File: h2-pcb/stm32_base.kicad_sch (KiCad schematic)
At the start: 41 parts, among them J1 Network Connector, J2 STDC14, SW1 SW_Push, U1 LD39050PU33R, U2 STM32G474RBT6, U3 SN65HVD230, Y1 8MHz

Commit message: Added Mosfets and LEDs
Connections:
- net PA6: now reaches U2.20 (PA6)
- net PA7: now reaches U2.21 (PA7)
- net PB0: now reaches U2.24 (PB0)
- net PB1: now reaches U2.25 (PB1)
- net PB2: now reaches U2.26 (PB2)
- net PA8: now reaches U2.42 (PA8)
- no-connect marks 37 -> 31
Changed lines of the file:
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@@
-	)
-	(no_connect
-		(at 99.06 110.49)
 	)
 	(no_connect
@@
 	)
 	(no_connect
-		(at 99.06 143.51)
-	)
-	(no_connect
 		(at 99.06 163.83)
 	)
@@
 	)
 	(no_connect
-		(at 99.06 115.57)
-	)
-	(no_connect
 		(at 63.5 138.43)
 	)
@@
 	)
 	(no_connect
-		(at 99.06 140.97)
-	)
-	(no_connect
-		(at 99.06 138.43)
-	)
-	(no_connect
 		(at 99.06 176.53)
 	)
@@
 	)
 	(no_connect
-		(at 99.06 113.03)
-	)
-	(no_connect
 		(at 99.06 161.29)
 	)
@@
 	(wire
 		(pts
+			(xy 99.06 118.11) (xy 101.6 118.11)
+		)
+		(stroke
+			(width 0)
+			(type default)
+		)
+	)
+	(wire
+		(pts
 			(xy 99.06 102.87) (xy 115.57 102.87)
 		)
@@
 	(wire
 		(pts
-			(xy 99.06 118.11) (xy 101.6 118.11)
-		)
-		(stroke
-			(width 0)
-			(type default)
-		)
-	)
-	(wire
-		(pts
 			(xy 146.05 142.24) (xy 146.05 143.51)
 		)
@@
 	(wire
 		(pts
+			(xy 99.06 143.51) (xy 101.6 143.51)
+		)
+		(stroke
+			(width 0)
+			(type default)
+		)
+	)
+	(wire
+		(pts
 			(xy 276.86 90.17) (xy 260.35 90.17)
 		)
@@
 	(wire
 		(pts
+			(xy 99.06 140.97) (xy 101.6 140.97)
+		)
+		(stroke
+			(width 0)
+			(type default)
+		)
+	)
+	(wire
+		(pts
 			(xy 276.86 107.95) (xy 260.35 107.95)
 		)
@@
 	(wire
 		(pts
+			(xy 99.06 113.03) (xy 101.6 113.03)
+		)
+		(stroke
+			(width 0)
+			(type default)
+		)
+	)
+	(wire
+		(pts
 			(xy 135.89 74.93) (xy 135.89 76.2)
 		)
@@
 	(wire
 		(pts
+			(xy 99.06 115.57) (xy 101.6 115.57)
+		)
+		(stroke
+			(width 0)
+			(type default)
+		)
+	)
+	(wire
+		(pts
 			(xy 83.82 87.63) (xy 83.82 86.36)
 		)
@@
 	(wire
 		(pts
+			(xy 99.06 110.49) (xy 101.6 110.49)
+		)
+		(stroke
+			(width 0)
+			(type default)
+		)
+	)
+	(wire
+		(pts
 			(xy 135.89 142.24) (xy 137.16 142.24)
 		)
@@
 		(pts
 			(xy 109.22 158.75) (xy 109.22 160.02)
+		)
+		(stroke
+			(width 0)
+			(type default)
+		)
+	)
+	(wire
+		(pts
+			(xy 99.06 138.43) (xy 101.6 138.43)
 		)
 		(stroke
@@
 			)
 			(justify right bottom)
+		)
+	)
+	(hierarchical_label "PB2"
+		(shape output)
+		(at 101.6 143.51 0)
+		(effects
+			(font
+				(size 1.27 1.27)
+			)
+			(justify left)
 		)
 	)
@@
 		)
 	)
+	(hierarchical_label "PA6"
+		(shape output)
+		(at 101.6 110.49 0)
+		(effects
+			(font
+				(size 1.27 1.27)
+			)
+			(justify left)
+		)
+	)
+	(hierarchical_label "PA8"
+		(shape output)
+		(at 101.6 115.57 0)
+		(effects
+			(font
+				(size 1.27 1.27)
+			)
+			(justify left)
+		)
+	)
+	(hierarchical_label "PA7"
+		(shape output)
+		(at 101.6 113.03 0)
+		(effects
+			(font
+				(size 1.27 1.27)
+			)
+			(justify left)
+		)
+	)
 	(hierarchical_label "PA9"
 		(shape output)
@@
 		)
 	)
+	(hierarchical_label "PB1"
+		(shape output)
+		(at 101.6 140.97 0)
+		(effects
+			(font
+				(size 1.27 1.27)
+			)
+			(justify left)
+		)
+	)
 	(hierarchical_label "PA5"
 		(shape output)
@@
 		(effects
 			(font
+				(size 1.27 1.27)
+			)
+			(justify left)
+		)
+	)
+	(hierarchical_label "PB0"
+		(shape output)
+		(at 101.6 138.43 0)
+		(effects
+			(font

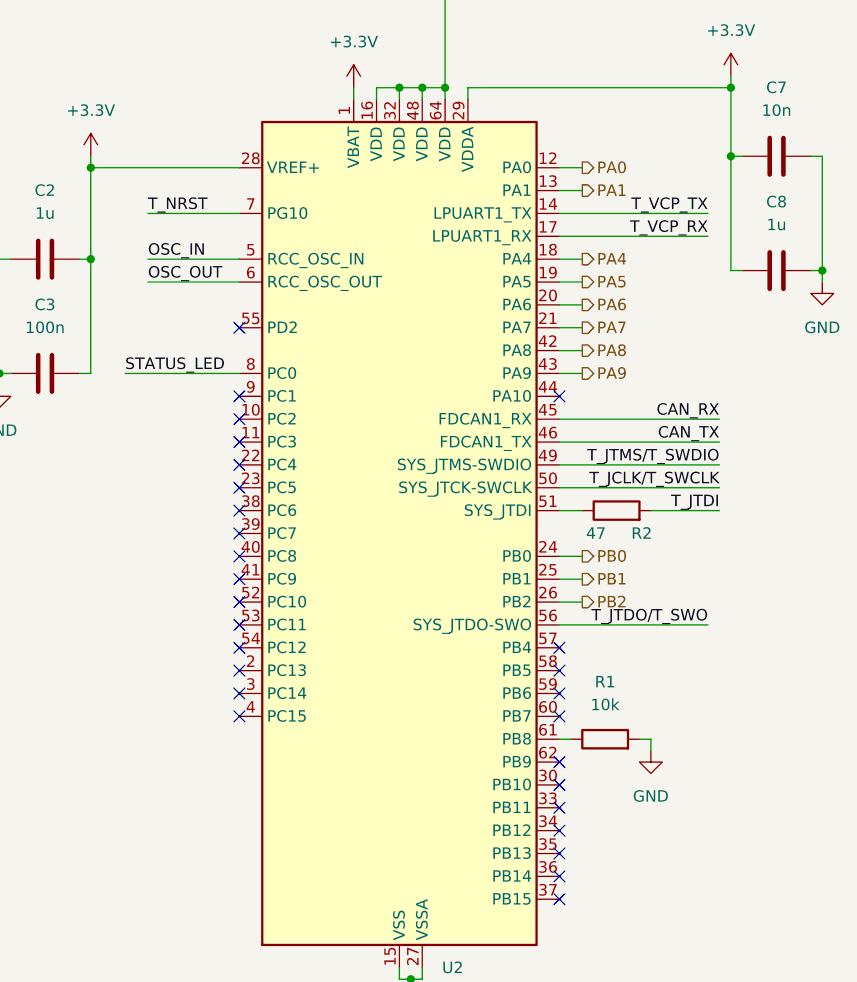
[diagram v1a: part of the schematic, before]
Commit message: h2-pcb: implement review comments in schematic
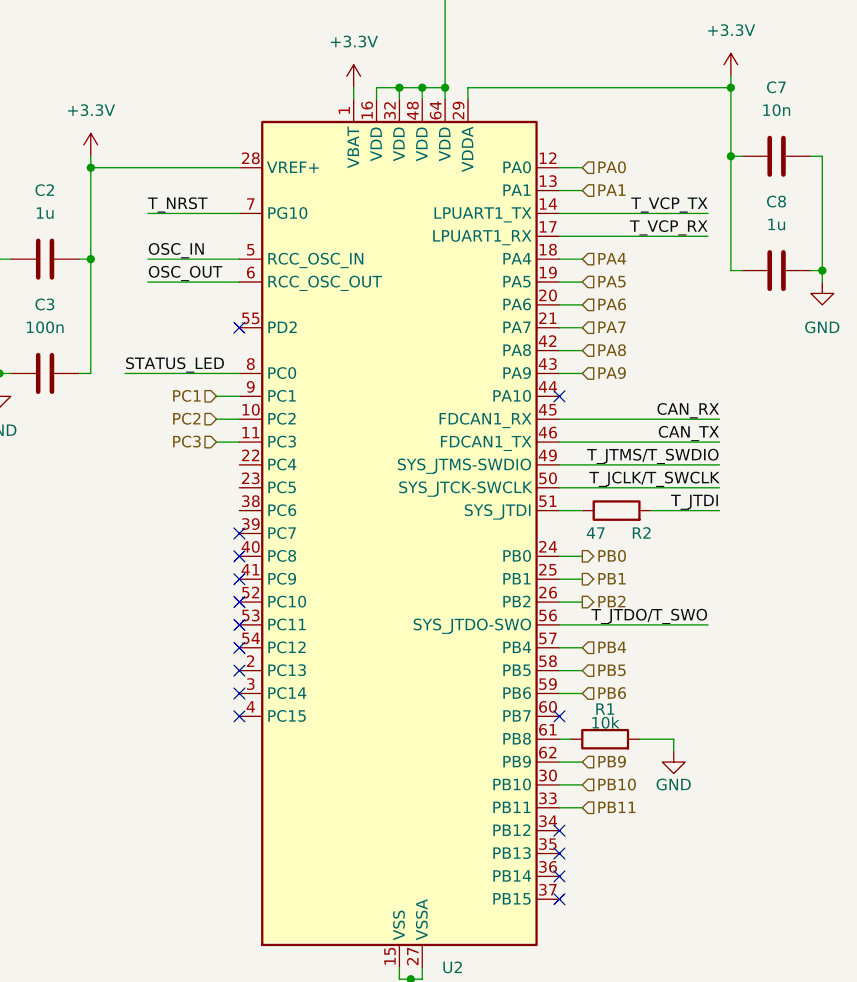
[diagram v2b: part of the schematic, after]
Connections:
- net PC2: now reaches U2.10 (PC2)
- net PC3: now reaches U2.11 (PC3)
- net PB10: now reaches U2.30 (PB10)
- net PB11: now reaches U2.33 (PB11)
- net PB4: now reaches U2.57 (PB4)
- net PB5: now reaches U2.58 (PB5)
- net PB6: now reaches U2.59 (PB6)
- net PB9: now reaches U2.62 (PB9)
- net PC1: now reaches U2.9 (PC1)
- no-connect marks 31 -> 19
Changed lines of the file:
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@@
 	)
 	(no_connect
-		(at 99.06 163.83)
-	)
-	(no_connect
 		(at 99.06 120.65)
 	)
 	(no_connect
-		(at 99.06 148.59)
-	)
-	(no_connect
 		(at 260.35 100.33)
 	)
@@
 	)
 	(no_connect
-		(at 99.06 151.13)
-	)
-	(no_connect
 		(at 74.93 31.75)
 	)
@@
 	)
 	(no_connect
-		(at 99.06 153.67)
-	)
-	(no_connect
-		(at 63.5 128.27)
-	)
-	(no_connect
-		(at 63.5 120.65)
-	)
-	(no_connect
-		(at 63.5 130.81)
-	)
-	(no_connect
-		(at 63.5 133.35)
-	)
-	(no_connect
 		(at 99.06 176.53)
 	)
@@
 	)
 	(no_connect
-		(at 63.5 125.73)
-	)
-	(no_connect
 		(at 63.5 135.89)
 	)
 	(no_connect
-		(at 99.06 161.29)
-	)
-	(no_connect
-		(at 63.5 123.19)
-	)
-	(no_connect
-		(at 99.06 166.37)
-	)
-	(no_connect
 		(at 99.06 173.99)
 	)
@@
 	(wire
 		(pts
-			(xy 107.95 158.75) (xy 109.22 158.75)
+			(xy 107.95 158.75) (xy 111.76 158.75)
 		)
 		(stroke
@@
 	(wire
 		(pts
+			(xy 99.06 161.29) (xy 101.6 161.29)
+		)
+		(stroke
+			(width 0)
+			(type default)
+		)
+	)
+	(wire
+		(pts
 			(xy 186.69 69.85) (xy 196.85 69.85)
 		)
@@
 	(wire
 		(pts
+			(xy 99.06 163.83) (xy 101.6 163.83)
+		)
+		(stroke
+			(width 0)
+			(type default)
+		)
+	)
+	(wire
+		(pts
 			(xy 243.84 147.32) (xy 243.84 148.59)
 		)
@@
 	(wire
 		(pts
+			(xy 60.96 123.19) (xy 63.5 123.19)
+		)
+		(stroke
+			(width 0)
+			(type default)
+		)
+	)
+	(wire
+		(pts
 			(xy 276.86 107.95) (xy 260.35 107.95)
 		)
@@
 	(wire
 		(pts
+			(xy 60.96 120.65) (xy 63.5 120.65)
+		)
+		(stroke
+			(width 0)
+			(type default)
+		)
+	)
+	(wire
+		(pts
 			(xy 78.74 87.63) (xy 78.74 86.36)
 		)
@@
 	(wire
 		(pts
+			(xy 99.06 148.59) (xy 101.6 148.59)
+		)
+		(stroke
+			(width 0)
+			(type default)
+		)
+	)
+	(wire
+		(pts
 			(xy 135.89 104.14) (xy 137.16 104.14)
 		)
@@
 	(wire
 		(pts
+			(xy 99.06 166.37) (xy 101.6 166.37)
+		)
+		(stroke
+			(width 0)
+			(type default)
+		)
+	)
+	(wire
+		(pts
 			(xy 144.78 116.84) (xy 146.05 116.84)
 		)
@@
 	(wire
 		(pts
+			(xy 60.96 125.73) (xy 63.5 125.73)
+		)
+		(stroke
+			(width 0)
+			(type default)
+		)
+	)
+	(wire
+		(pts
 			(xy 149.86 49.53) (xy 149.86 48.26)
 		)
@@
 	(wire
 		(pts
+			(xy 99.06 153.67) (xy 101.6 153.67)
+		)
+		(stroke
+			(width 0)
+			(type default)
+		)
+	)
+	(wire
+		(pts
 			(xy 83.82 87.63) (xy 83.82 86.36)
 		)
@@
 	(wire
 		(pts
+			(xy 99.06 151.13) (xy 101.6 151.13)
+		)
+		(stroke
+			(width 0)
+			(type default)
+		)
+	)
+	(wire
+		(pts
 			(xy 204.47 69.85) (xy 214.63 69.85)
 		)
@@
 	(wire
 		(pts
-			(xy 109.22 158.75) (xy 109.22 160.02)
+			(xy 111.76 158.75) (xy 111.76 160.02)
 		)
 		(stroke
@@
 		)
 	)
+	(hierarchical_label "PB11"
+		(shape input)
+		(at 101.6 166.37 0)
+		(effects
+			(font
+				(size 1.27 1.27)
+			)
+			(justify left)
+		)
+	)
 	(hierarchical_label "PB2"
 		(shape output)
@@
 	)
 	(hierarchical_label "PA1"
-		(shape output)
+		(shape input)
 		(at 101.6 97.79 0)
 		(effects
@@
 		)
 	)
+	(hierarchical_label "PB5"
+		(shape input)
+		(at 101.6 151.13 0)
+		(effects
+			(font
+				(size 1.27 1.27)
+			)
+			(justify left)
+		)
+	)
+	(hierarchical_label "PC1"
+		(shape input)
+		(at 60.96 120.65 180)
+		(effects
+			(font
+				(size 1.27 1.27)
+			)
+			(justify right)
+		)
+	)
+	(hierarchical_label "PB6"
+		(shape input)
+		(at 101.6 153.67 0)
+		(effects
+			(font
+				(size 1.27 1.27)
+			)
+			(justify left)
+		)
+	)
 	(hierarchical_label "PA6"
-		(shape output)
+		(shape input)
 		(at 101.6 110.49 0)
 		(effects
@@
 	)
 	(hierarchical_label "PA8"
-		(shape output)
+		(shape input)
 		(at 101.6 115.57 0)
 		(effects
@@
 		)
 	)
+	(hierarchical_label "PC2"
+		(shape input)
+		(at 60.96 123.19 180)
+		(effects
+			(font
+				(size 1.27 1.27)
+			)
+			(justify right)
+		)
+	)
 	(hierarchical_label "PA7"
-		(shape output)
+		(shape input)
 		(at 101.6 113.03 0)
 		(effects
@@
 		)
 	)
+	(hierarchical_label "PB9"
+		(shape input)
+		(at 101.6 161.29 0)
+		(effects
+			(font
+				(size 1.27 1.27)
+			)
+			(justify left)
+		)
+	)
 	(hierarchical_label "PA9"
-		(shape output)
+		(shape input)
 		(at 101.6 118.11 0)
 		(effects
@@
 		)
 	)
+	(hierarchical_label "PB10"
+		(shape input)
+		(at 101.6 163.83 0)
+		(effects
+			(font
+				(size 1.27 1.27)
+			)
+			(justify left)
+		)
+	)
 	(hierarchical_label "PA4"
-		(shape output)
+		(shape input)
 		(at 101.6 105.41 0)
 		(effects
@@
 	)
 	(hierarchical_label "PA0"
-		(shape output)
+		(shape input)
 		(at 101.6 95.25 0)
 		(effects
@@
 		)
 	)
+	(hierarchical_label "PC3"
+		(shape input)
+		(at 60.96 125.73 180)
+		(effects
+			(font
+				(size 1.27 1.27)
+			)
+			(justify right)
+		)
+	)
+	(hierarchical_label "PB4"
+		(shape input)
+		(at 101.6 148.59 0)
+		(effects
+			(font
+				(size 1.27 1.27)
+			)
+			(justify left)
+		)
+	)
 	(hierarchical_label "PB1"
 		(shape output)
@@
 	)
 	(hierarchical_label "PA5"
-		(shape output)
+		(shape input)
 		(at 101.6 107.95 0)
 		(effects
@@
 		(on_board yes)
 		(dnp no)
-		(fields_autoplaced yes)
 		(property "Reference" "R1"
-			(at 104.14 152.4 90)
+			(at 104.14 155.448 90)
 			(effects
 				(font
@@
 		)
 		(property "Value" "10k"
-			(at 104.14 154.94 90)
+			(at 104.14 156.972 90)
 			(effects
 				(font
@@
 	(symbol
 		(lib_id "power:GND")
-		(at 109.22 160.02 0)
+		(at 111.76 160.02 0)
 		(unit 1)
 		(exclude_from_sim no)
@@
 		(on_board yes)
 		(dnp no)
-		(fields_autoplaced yes)
 		(property "Reference" "#PWR08"
-			(at 109.22 166.37 0)
+			(at 111.76 166.37 0)
 			(effects
 				(font
@@
 		)
 		(property "Value" "GND"
-			(at 109.22 165.1 0)
+			(at 111.76 163.83 0)
 			(effects
 				(font
@@
 		)
 		(property "Footprint" ""
-			(at 109.22 160.02 0)
+			(at 111.76 160.02 0)
 			(effects
 				(font
@@
 		)
 		(property "Datasheet" ""
-			(at 109.22 160.02 0)
+			(at 111.76 160.02 0)
 			(effects
 				(font
@@
 		)
 		(property "Description" "Power symbol creates a global label with name \"GND\" , ground"
-			(at 109.22 160.02 0)
+			(at 111.76 160.02 0)
 			(effects
 				(font

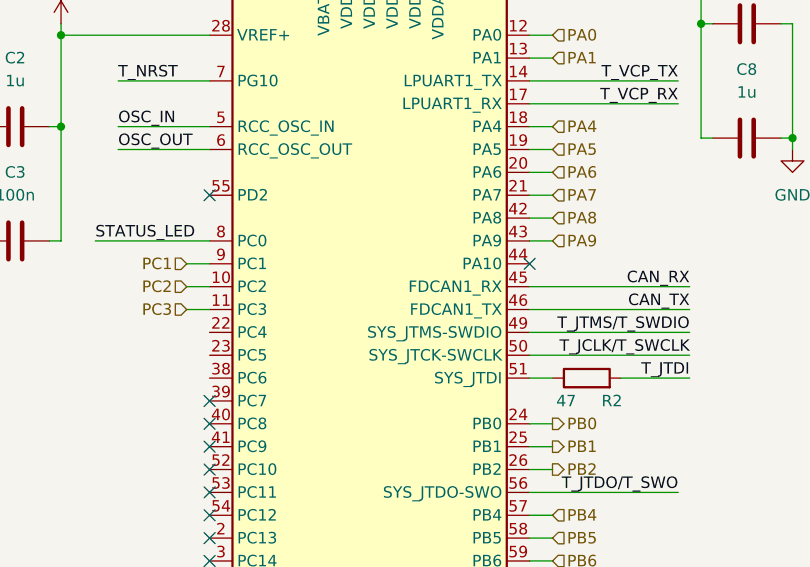
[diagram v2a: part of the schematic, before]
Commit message: h2-pcb: implement review comments in schematic 2.0
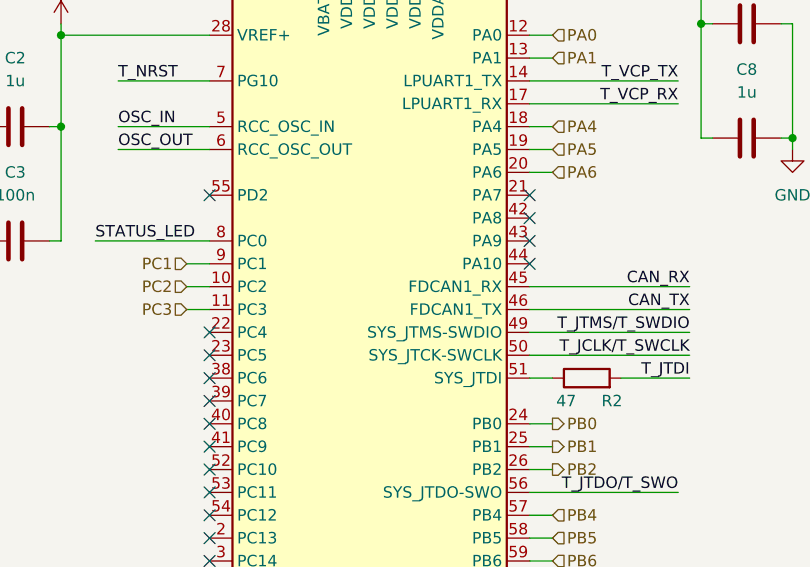
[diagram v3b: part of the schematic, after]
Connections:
- net PA7: no longer names the net of U2.21 (PA7)
- net PA8: no longer names the net of U2.42 (PA8)
- net PA9: no longer names the net of U2.43 (PA9)
- no-connect marks 19 -> 25
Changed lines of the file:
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@@
+	)
+	(no_connect
+		(at 99.06 115.57)
 	)
 	(no_connect
@@
 	)
 	(no_connect
+		(at 63.5 130.81)
+	)
+	(no_connect
 		(at 99.06 171.45)
 	)
@@
 	)
 	(no_connect
+		(at 63.5 128.27)
+	)
+	(no_connect
 		(at 99.06 120.65)
 	)
@@
 	)
 	(no_connect
+		(at 99.06 118.11)
+	)
+	(no_connect
+		(at 63.5 133.35)
+	)
+	(no_connect
 		(at 99.06 176.53)
 	)
@@
 	)
 	(no_connect
+		(at 99.06 113.03)
+	)
+	(no_connect
 		(at 99.06 173.99)
 	)
@@
 	(wire
 		(pts
-			(xy 99.06 118.11) (xy 101.6 118.11)
-		)
-		(stroke
-			(width 0)
-			(type default)
-		)
-	)
-	(wire
-		(pts
 			(xy 99.06 102.87) (xy 115.57 102.87)
 		)
@@
 	(wire
 		(pts
-			(xy 99.06 113.03) (xy 101.6 113.03)
-		)
-		(stroke
-			(width 0)
-			(type default)
-		)
-	)
-	(wire
-		(pts
 			(xy 135.89 74.93) (xy 135.89 76.2)
 		)
@@
 		(pts
 			(xy 81.28 36.83) (xy 81.28 35.56)
-		)
-		(stroke
-			(width 0)
-			(type default)
-		)
-	)
-	(wire
-		(pts
-			(xy 99.06 115.57) (xy 101.6 115.57)
 		)
 		(stroke
@@
 		)
 	)
-	(hierarchical_label "PA8"
-		(shape input)
-		(at 101.6 115.57 0)
-		(effects
-			(font
-				(size 1.27 1.27)
-			)
-			(justify left)
-		)
-	)
 	(hierarchical_label "PC2"
 		(shape input)
@@
 		)
 	)
-	(hierarchical_label "PA7"
-		(shape input)
-		(at 101.6 113.03 0)
-		(effects
-			(font
-				(size 1.27 1.27)
-			)
-			(justify left)
-		)
-	)
 	(hierarchical_label "PB9"
 		(shape input)
@@
 		(effects
 			(font
-				(size 1.27 1.27)
-			)
-			(justify left)
-		)
-	)
-	(hierarchical_label "PA9"
-		(shape input)
-		(at 101.6 118.11 0)
-		(effects
-			(font

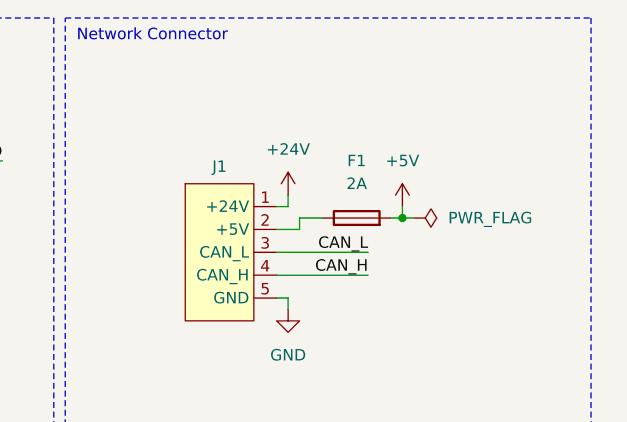
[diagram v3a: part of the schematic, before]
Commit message: h2-pcb: Added fuse to +24V network connector pin in schematic
Added a safety fuse of 5A to the +24V network connector pin
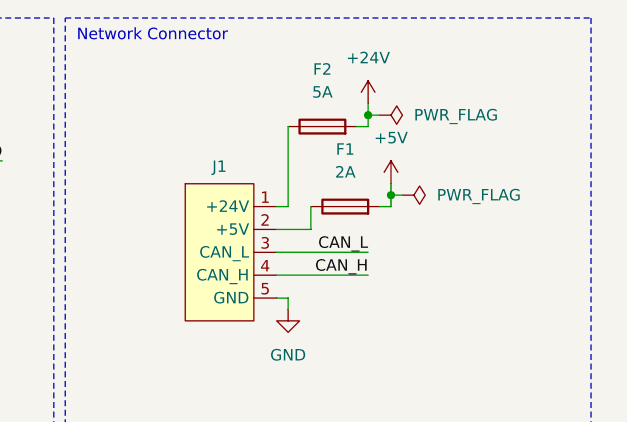
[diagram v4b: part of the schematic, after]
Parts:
- added F2: 5A, symbol Device:Fuse
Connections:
- net +24V: now also F2.2; no longer J1.1 (+24V)
- new net: F2.1, J1.1 (+24V)
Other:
- moved on the sheet: F1

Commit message: h2-pcb:Added footprint to 5A Fuse
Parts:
- F2: footprint (none) -> Exocet:Fuse_Holder_Littelfuse_01530008
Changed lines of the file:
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@@
 			)
 		)
-		(property "Footprint" ""
+		(property "Footprint" "Exocet:Fuse_Holder_Littelfuse_01530008"
 			(at 254 27.178 90)
 			(effects
